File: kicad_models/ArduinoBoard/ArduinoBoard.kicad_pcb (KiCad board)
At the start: 2 copper layers, 90.5 x 70 mm, 20 parts, among them J1 5V Output, J2 Buttons, J3 PWM Output, J4 12V Input, J5 Conn_01x04_Pin, J6 Conn_01x04_Pin, J7 Conn_01x06_Pin, J8 Conn_01x06_Pin, SW1 SW_Push_Dual, SW2 SW_Push_Dual

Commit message: A couple of small changes to the PCB prior to printing.
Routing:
- net /GND: track 165.3 -> 164.0 mm
- net Net-(A1-+5V): track 102.0 -> 100.8 mm

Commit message: Started to make a 3D printable face plate with Solid Edge. Also added another child board (OLED) that allows a hole to be drilled for a 12mm momentary on-off-on switch (rather than buttons) - this update requires the user so wire the switch with the screwdown terminals rather than with traces on the board. The parent board (Arduino) didn't change apart from scooting the Arduino to one side slightly to make room for the back of the switch.
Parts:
- added A1: Arduino_Nano_v3.x, Module:Arduino_Nano, F.Cu at (109.3, 107.5)
- added H1: MountingHole, MountingHole:MountingHole_2.2mm_M2_DIN965_Pad, F.Cu at (79.5, 63.5)
- added H2: MountingHole, MountingHole:MountingHole_2.2mm_M2_DIN965_Pad, F.Cu at (127.5, 63.5)
- added H3: MountingHole, MountingHole:MountingHole_2.2mm_M2_DIN965_Pad, F.Cu at (127.5, 129.5)
- added H4: MountingHole, MountingHole:MountingHole_2.2mm_M2_DIN965_Pad, F.Cu at (79.5, 129.5)
- added H5: MountingHole, MountingHole:MountingHole_2.2mm_M2_DIN965_Pad, F.Cu at (73.8, 81.5)
- added H6: MountingHole, MountingHole:MountingHole_2.2mm_M2_DIN965_Pad, F.Cu at (73.8, 129.5)
- added H7: MountingHole, MountingHole:MountingHole_2.2mm_M2_DIN965_Pad, F.Cu at (41.4, 81.5)
- added H8: MountingHole, MountingHole:MountingHole_2.2mm_M2_DIN965_Pad, F.Cu at (41.4, 129.5)
- added J1: 5V Output, TerminalBlock:TerminalBlock_bornier-2_P5.08mm, F.Cu at (118.1, 88.8)
- added J10: Conn_01x06_Pin, Connector_PinHeader_2.54mm:PinHeader_1x06_P2.54mm_Vertical, F.Cu at (40.8, 111.8)
- added J2: Buttons, TerminalBlock:TerminalBlock_bornier-2_P5.08mm, F.Cu at (118.1, 78.6)
- added J3: PWM Output, TerminalBlock:TerminalBlock_bornier-2_P5.08mm, F.Cu at (118.1, 68.5)
- added J4: 12V Input, TerminalBlock:TerminalBlock_bornier-2_P5.08mm, F.Cu at (118.1, 103.8)
- added J5: Conn_01x04_Pin, Connector_PinHeader_2.54mm:PinHeader_1x04_P2.54mm_Vertical, F.Cu at (94.1, 113.8)
- added J7: Conn_01x06_Pin, Connector_PinHeader_2.54mm:PinHeader_1x06_P2.54mm_Vertical, F.Cu at (109.8, 130.1)
- added J9: Conn_01x04_Pin, Connector_PinHeader_2.54mm:PinHeader_1x04_P2.54mm_Vertical, F.Cu at (54.2, 102.1)
- added TH1: Thermistor_NTC, Resistor_THT:R_Axial_DIN0204_L3.6mm_D1.6mm_P5.08mm_Vertical, F.Cu at (116.3, 121.2)
- moved A1 117.2 mm to (235.5, 107.3)
- moved H5 116.1 mm to (200.0, 81.3)
- moved H6 116.1 mm to (200.0, 129.3)
- moved H7 116.1 mm to (167.6, 81.3)
- moved H8 116.1 mm to (167.6, 129.3)
- moved J8 116.1 mm to (167.0, 111.7)
- moved SW1 116.1 mm to (186.0, 87.5)
- moved SW2 116.1 mm to (169.2, 87.5)
- moved J6 116.1 mm to (180.4, 102.1)
- moved J1 115.7 mm to (244.3, 88.7)
- moved J3 115.7 mm to (244.3, 68.3)
- moved TH1 115.7 mm to (242.5, 121.0)
- moved H1 115.7 mm to (205.7, 63.3)
- moved H2 115.7 mm to (253.7, 63.3)
- moved H3 115.7 mm to (253.7, 129.3)
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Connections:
- net OLED_Board_5V renamed Net-(J6-Pin_2)
- net OLED_Board_Extend_Button renamed Net-(J8-Pin_6)
- net OLED_Board_GND renamed Net-(J6-Pin_1)
- J8 pad 5: OLED_Board_Retract_Button -> Net-(J8-Pin_5)
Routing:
- net /GND: track 164.0 -> 325.1 mm
- net Net-(A1-D3): track 147.7 -> 293.5 mm
- net Net-(A1-D2): track 146.6 -> 288.3 mm
- net Net-(A1-+5V): track 100.8 -> 204.8 mm
- net Net-(A1-A4): track 58.1 -> 119.4 mm
- net Net-(A1-A5): track 56.1 -> 115.3 mm
- net Net-(A1-A2): track 54.0 -> 106.4 mm
- net Net-(J10-Pin_4): track 0.00 -> 26.4 mm
- net /VI+: track 24.9 -> 49.8 mm
- net Net-(J10-Pin_3): track 0.00 -> 23.9 mm
- net OLED_Board_Retract_Button: track 22.7 -> 0.00 mm
- net Net-(J8-Pin_5): track 12.5 -> 35.2 mm
- net /VO+: track 19.3 -> 41.7 mm
- net Net-(J10-Pin_2): track 0.00 -> 21.4 mm
- net Net-(J10-Pin_1): track 0.00 -> 17.4 mm
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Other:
- board size 90.5 x 70 mm -> 216.3 x 70.2 mm

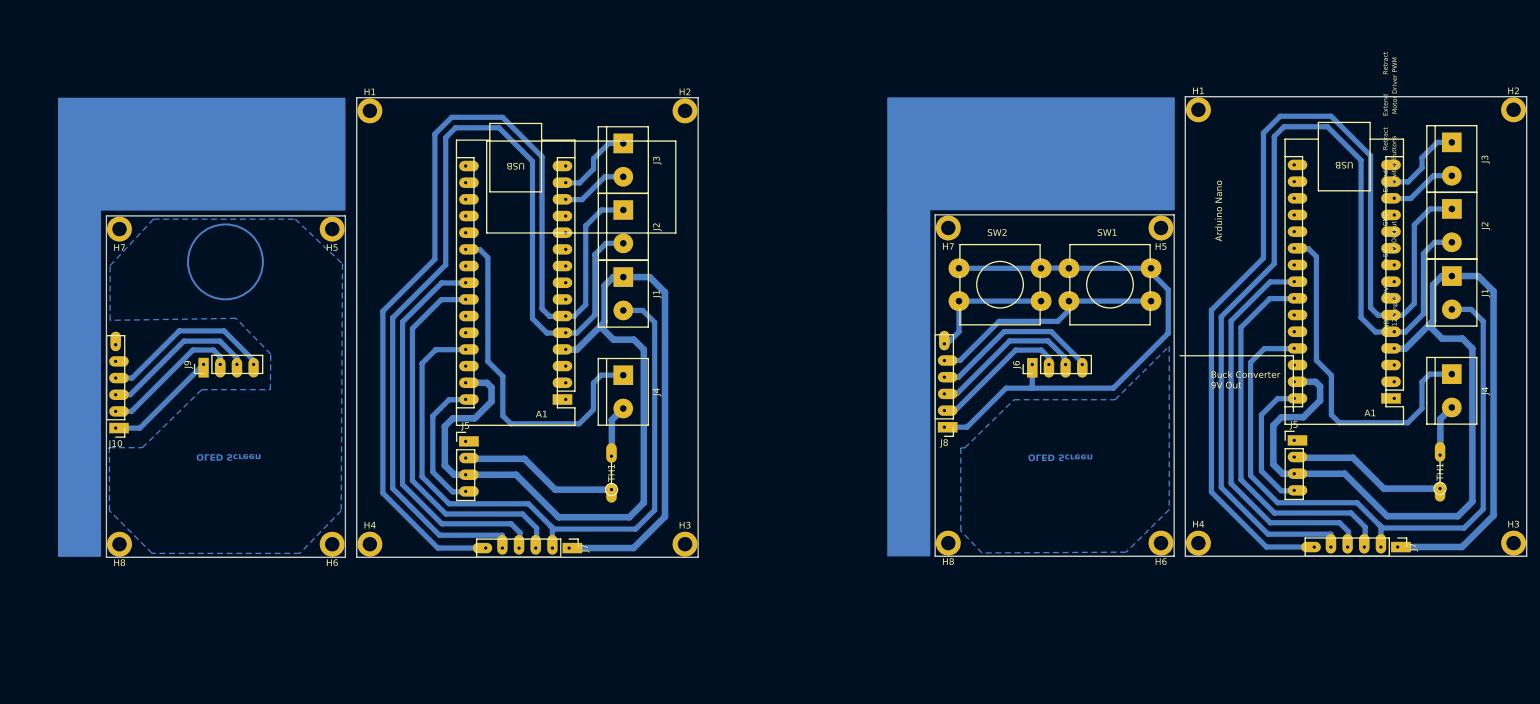
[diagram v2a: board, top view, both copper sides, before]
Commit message: Pushed the Arduino and other components slightly to the right to make a little more room for the switch.
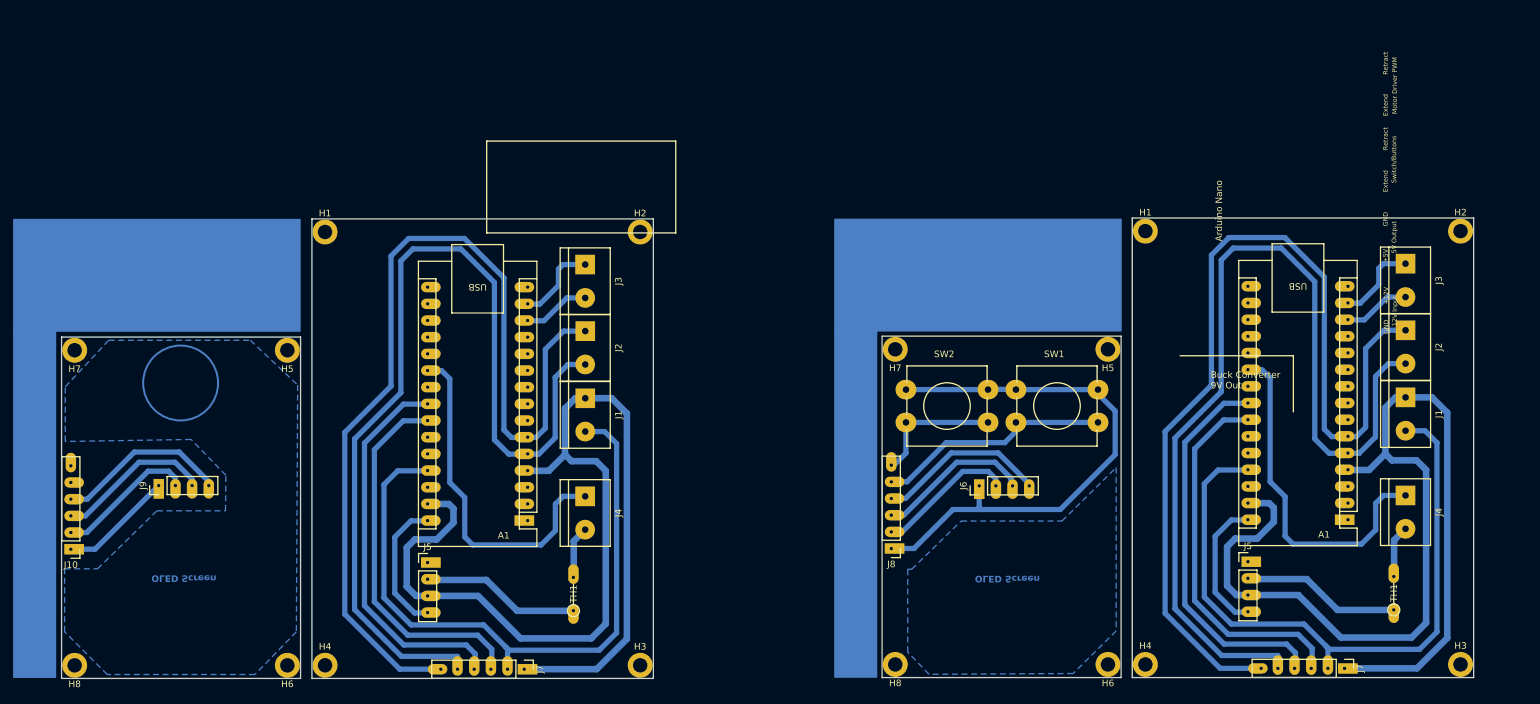
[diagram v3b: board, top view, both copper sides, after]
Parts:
- moved J6 20.2 mm to (172.3, 120.6)
- moved H5 20.2 mm to (191.9, 99.8)
- moved H6 20.2 mm to (191.9, 147.8)
- moved J8 20.2 mm to (158.9, 130.2)
- moved H1 20.2 mm to (197.6, 81.8)
- moved H2 20.2 mm to (245.6, 81.8)
- moved H3 20.2 mm to (245.6, 147.8)
- moved H4 20.2 mm to (197.6, 147.8)
- moved H7 20.2 mm to (159.5, 99.8)
- moved H8 20.2 mm to (159.5, 147.8)
- moved J7 20.2 mm to (228.0, 148.4)
- moved SW1 20.2 mm to (177.9, 106.0)
- moved SW2 20.2 mm to (161.2, 106.0)
- moved A1 19.8 mm to (228.5, 125.8)
- moved J1 19.8 mm to (237.2, 107.1)
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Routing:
- net /GND: track 325.1 -> 327.3 mm
- net Net-(A1-A5): track 115.3 -> 113.2 mm
- net Net-(A1-A4): track 119.4 -> 117.3 mm
- net Net-(A1-D2): track 288.3 -> 287.1 mm
- net Net-(A1-D3): track 293.5 -> 292.3 mm
- net Net-(A1-D11): track 24.4 -> 25.5 mm
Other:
- board size 216.3 x 70.2 mm -> 215.1 x 70.1 mm
